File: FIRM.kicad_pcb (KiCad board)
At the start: 4 copper layers, 40.5 x 40.5 mm, 98 parts, among them J2 DM3CS-SF, Q2 IRLML6402, U1 STM32F405RGTx, U2 MIC5219-3.3YM5, U6 A-USBC-20F0-EA-GSR05, U7 W25Q128JVS, X2 32.768khz, Y1 12 MHz

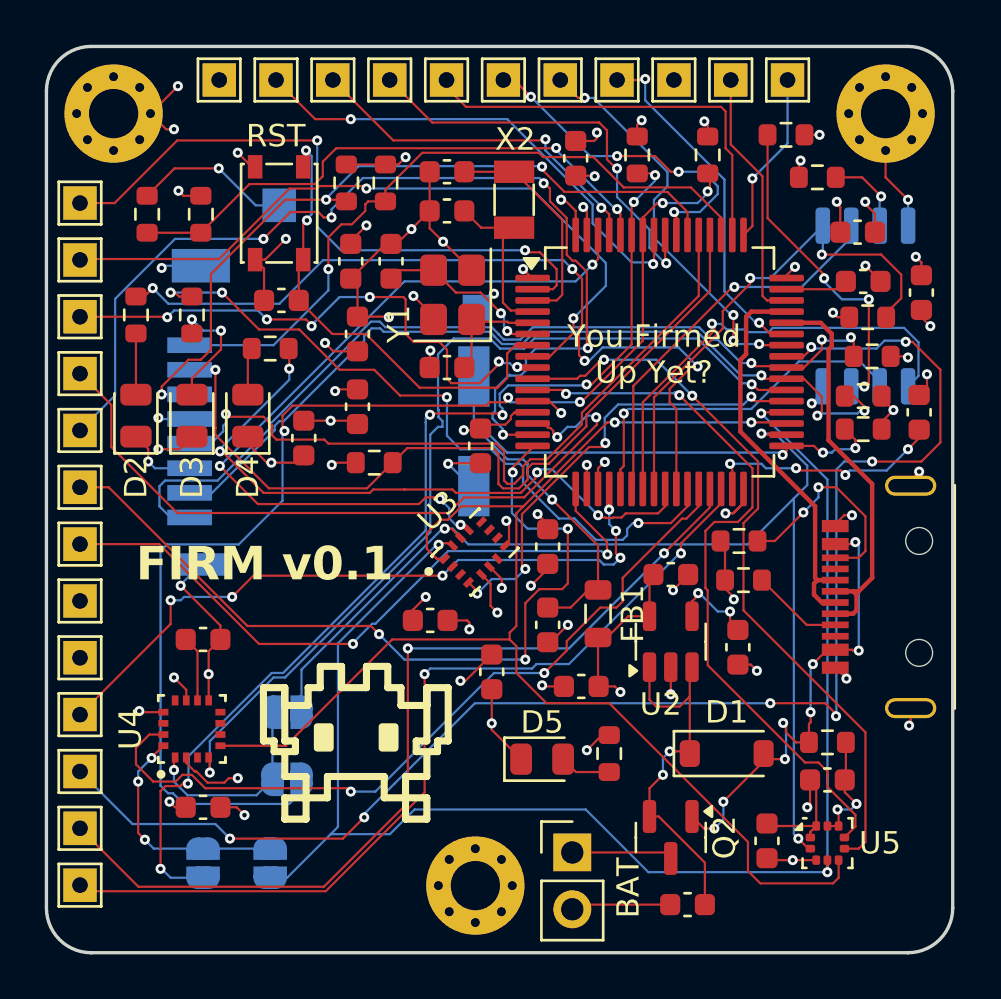
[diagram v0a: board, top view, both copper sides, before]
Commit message: Removed Jumpers from SCL & SDA of Magnetometer
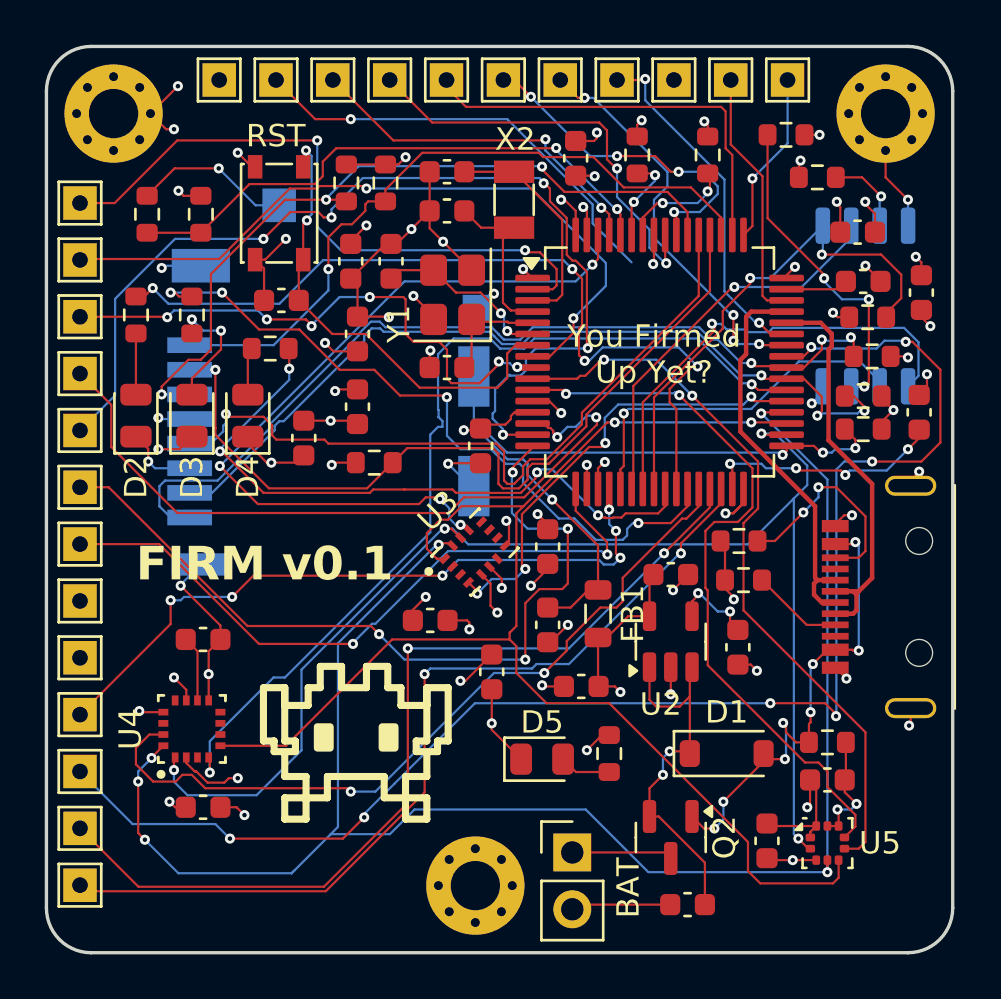
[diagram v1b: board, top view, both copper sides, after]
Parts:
- removed MOSI: SPI_SDI, Jumper:SolderJumper-2_P1.3mm_Open_RoundedPad1.0x1.5mm
- removed SCK: SPI_SCK, Jumper:SolderJumper-2_P1.3mm_Open_RoundedPad1.0x1.5mm
- removed SCL: I2C_SCL, Jumper:SolderJumper-2_P1.3mm_Open_RoundedPad1.0x1.5mm
- removed SDA: I2C_SDA, Jumper:SolderJumper-2_P1.3mm_Open_RoundedPad1.0x1.5mm
- D2: value LED -> LED_Blue
- D3: value LED -> LED_Yellow
- D4: value LED -> LED_Red
- D5: value LED -> LED_Green
- renumbered C13 to TP24
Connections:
- U4 pad 1: Net-(JP3-A) -> /SCK2
- U4 pad 16: Net-(JP1-A) -> /MOSI2
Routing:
- net /I2C1_SCL: track 55.9 -> 5.14 mm, vias 5 -> 2
- net /I2C1_SDA: track 47.7 -> 3.94 mm, vias 7 -> 2
- net /MOSI2: track 66.4 -> 77.5 mm, vias 3 -> 6
- net Net-(JP1-A): track 10.6 -> 0.00 mm, vias 3 -> 0
- net /SCK2: track 50.0 -> 59.6 mm, vias 3 -> 4
- net Net-(JP3-A): track 9.05 -> 0.00 mm, vias 1 -> 0
- net /PB5: track 22.1 -> 21.2 mm
